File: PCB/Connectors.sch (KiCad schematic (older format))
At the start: 0 parts

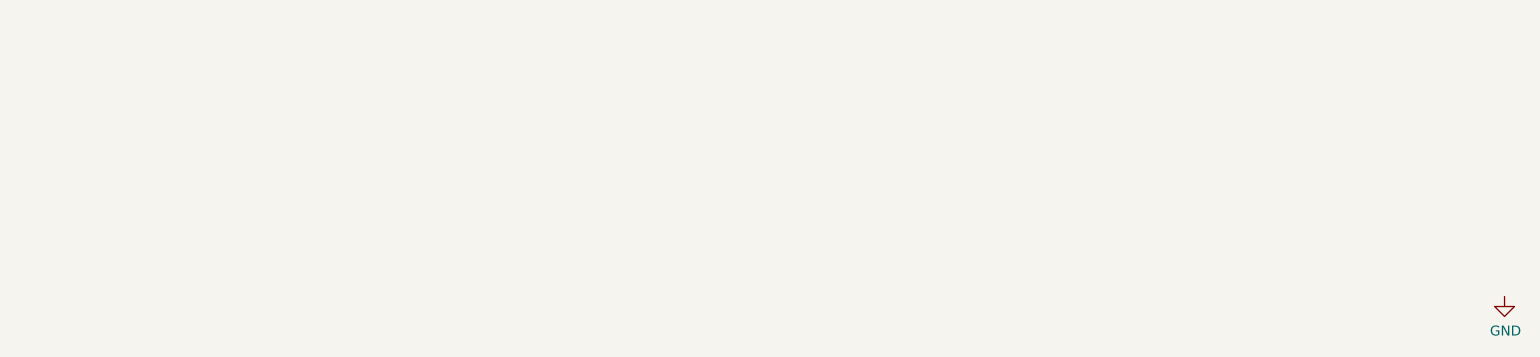
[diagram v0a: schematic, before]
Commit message: Added JST-PH connector to schematic
Orientation of JST-PH connector matches Adafruit Li-ion cells
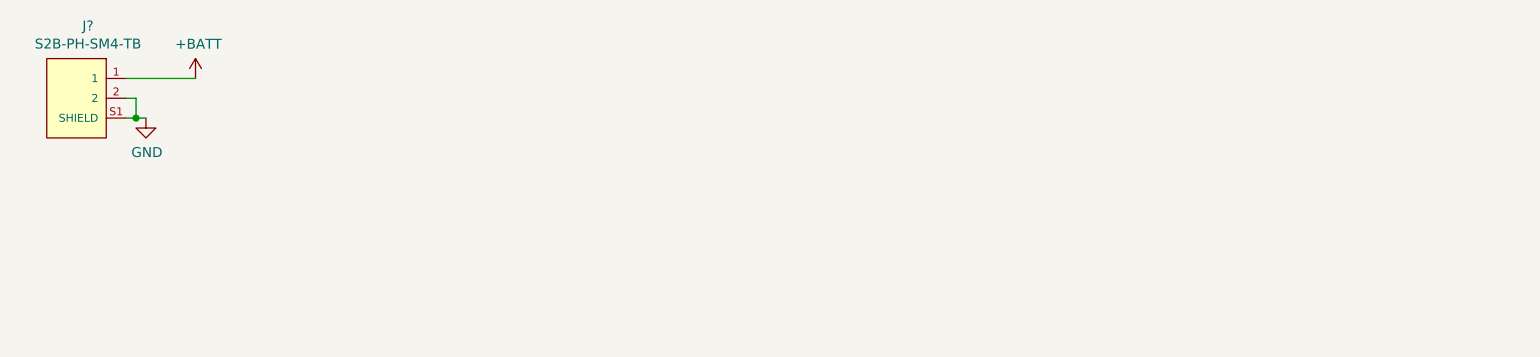
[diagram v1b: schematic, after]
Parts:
- added J?: S2B-PH-SM4-TB, Parts:JST_S2B-PH-SM4-TB, symbol Parts:S2B-PH-SM4-TB
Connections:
- net GND: now also J?.2, J?.S1 (SHIELD), J?.S2 (SHIELD)
- new net +BATT: J?.1
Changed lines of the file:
@@
 L power:GND #PWR?
 U 1 1 5DCE40E5
-P 8850 4100
-F 0 "#PWR?" H 8850 3850 50  0001 C CNN
-F 1 "GND" H 8855 3927 50  0000 C CNN
-F 2 "" H 8850 4100 50  0001 C CNN
-F 3 "" H 8850 4100 50  0001 C CNN
-	1    8850 4100
+P 2000 3200
+F 0 "#PWR?" H 2000 2950 50  0001 C CNN
+F 1 "GND" H 2005 3027 50  0000 C CNN
+F 2 "" H 2000 3200 50  0001 C CNN
+F 3 "" H 2000 3200 50  0001 C CNN
+	1    2000 3200
 	1    0    0    -1
 $EndComp
+$Comp
+L Parts:S2B-PH-SM4-TB J?
+U 1 1 5DCEC85E
+P 1650 3100
+F 0 "J?" H 1592 3465 50  0000 C CNN
+F 1 "S2B-PH-SM4-TB" H 1592 3374 50  0000 C CNN
+F 2 "Parts:JST_S2B-PH-SM4-TB" H 1650 2750 50  0001 C CNN
+F 3 "http://www.jst-mfg.com/product/detail_e.php?series=199" H 1700 3100 50  0001 L BNN
+	1    1650 3100
+	-1   0    0    -1
+$EndComp
+$Comp
+L power:+BATT #PWR?
+U 1 1 5DCED91D
+P 2250 3000
+F 0 "#PWR?" H 2250 2850 50  0001 C CNN
+F 1 "+BATT" H 2265 3173 50  0000 C CNN
+F 2 "" H 2250 3000 50  0001 C CNN
+F 3 "" H 2250 3000 50  0001 C CNN
+	1    2250 3000
+	1    0    0    -1
+$EndComp
+Wire Wire Line
+	1900 3000 2250 3000
+Wire Wire Line
+	1900 3200 1950 3200
+Wire Wire Line
+	1900 3100 1950 3100
+Wire Wire Line
+	1950 3100 1950 3200
+Connection ~ 1950 3200
+Wire Wire Line
+	1950 3200 2000 3200
 $EndSCHEMATC

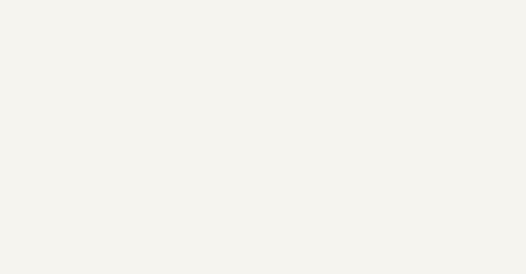
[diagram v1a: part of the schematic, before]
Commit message: Added "near radio" warning to microcontroller pins, connected more ICs to power rails, added transducer capacitive coupling
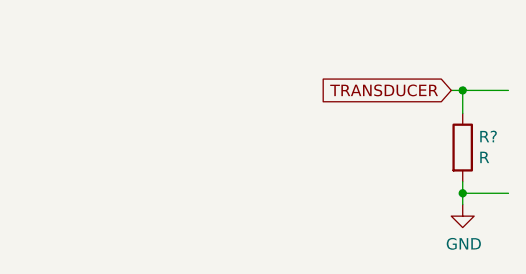
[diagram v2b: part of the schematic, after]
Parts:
- added R?: R, symbol Device:R
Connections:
- net labels added: TRANSDUCER
- wire segments 5 -> 11
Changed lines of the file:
@@
 $EndDescr
 $Comp
-L power:GND #PWR?
+L power:GND #PWR0130
 U 1 1 5DCE40E5
 P 2000 3200
-F 0 "#PWR?" H 2000 2950 50  0001 C CNN
+F 0 "#PWR0130" H 2000 2950 50  0001 C CNN
 F 1 "GND" H 2005 3027 50  0000 C CNN
 F 2 "" H 2000 3200 50  0001 C CNN
@@
 $EndComp
 $Comp
-L power:+BATT #PWR?
+L power:+BATT #PWR0131
 U 1 1 5DCED91D
 P 2250 3000
-F 0 "#PWR?" H 2250 2850 50  0001 C CNN
+F 0 "#PWR0131" H 2250 2850 50  0001 C CNN
 F 1 "+BATT" H 2265 3173 50  0000 C CNN
 F 2 "" H 2250 3000 50  0001 C CNN
@@
 Wire Wire Line
 	1950 3200 2000 3200
+Text GLabel 8400 3000 0    50   Input ~ 0
+TRANSDUCER
+$Comp
+L Device:R R?
+U 1 1 5DE80022
+P 8450 3250
+F 0 "R?" H 8520 3296 50  0000 L CNN
+F 1 "R" H 8520 3205 50  0000 L CNN
+F 2 "" V 8380 3250 50  0001 C CNN
+F 3 "~" H 8450 3250 50  0001 C CNN
+	1    8450 3250
+	1    0    0    -1
+$EndComp
+Wire Wire Line
+	8400 3000 8450 3000
+Wire Wire Line
+	8450 3000 8450 3100
+$Comp
+L power:GND #PWR?
+U 1 1 5DE80E0C
+P 8450 3500
+F 0 "#PWR?" H 8450 3250 50  0001 C CNN
+F 1 "GND" H 8455 3327 50  0000 C CNN
+F 2 "" H 8450 3500 50  0001 C CNN
+F 3 "" H 8450 3500 50  0001 C CNN
+	1    8450 3500
+	1    0    0    -1
+$EndComp
+Wire Wire Line
+	8450 3400 8450 3450
+Wire Wire Line
+	8450 3000 8650 3000
+Connection ~ 8450 3000
+Wire Wire Line
+	8450 3450 8650 3450
+Connection ~ 8450 3450
+Wire Wire Line
+	8450 3450 8450 3500
 $EndSCHEMATC

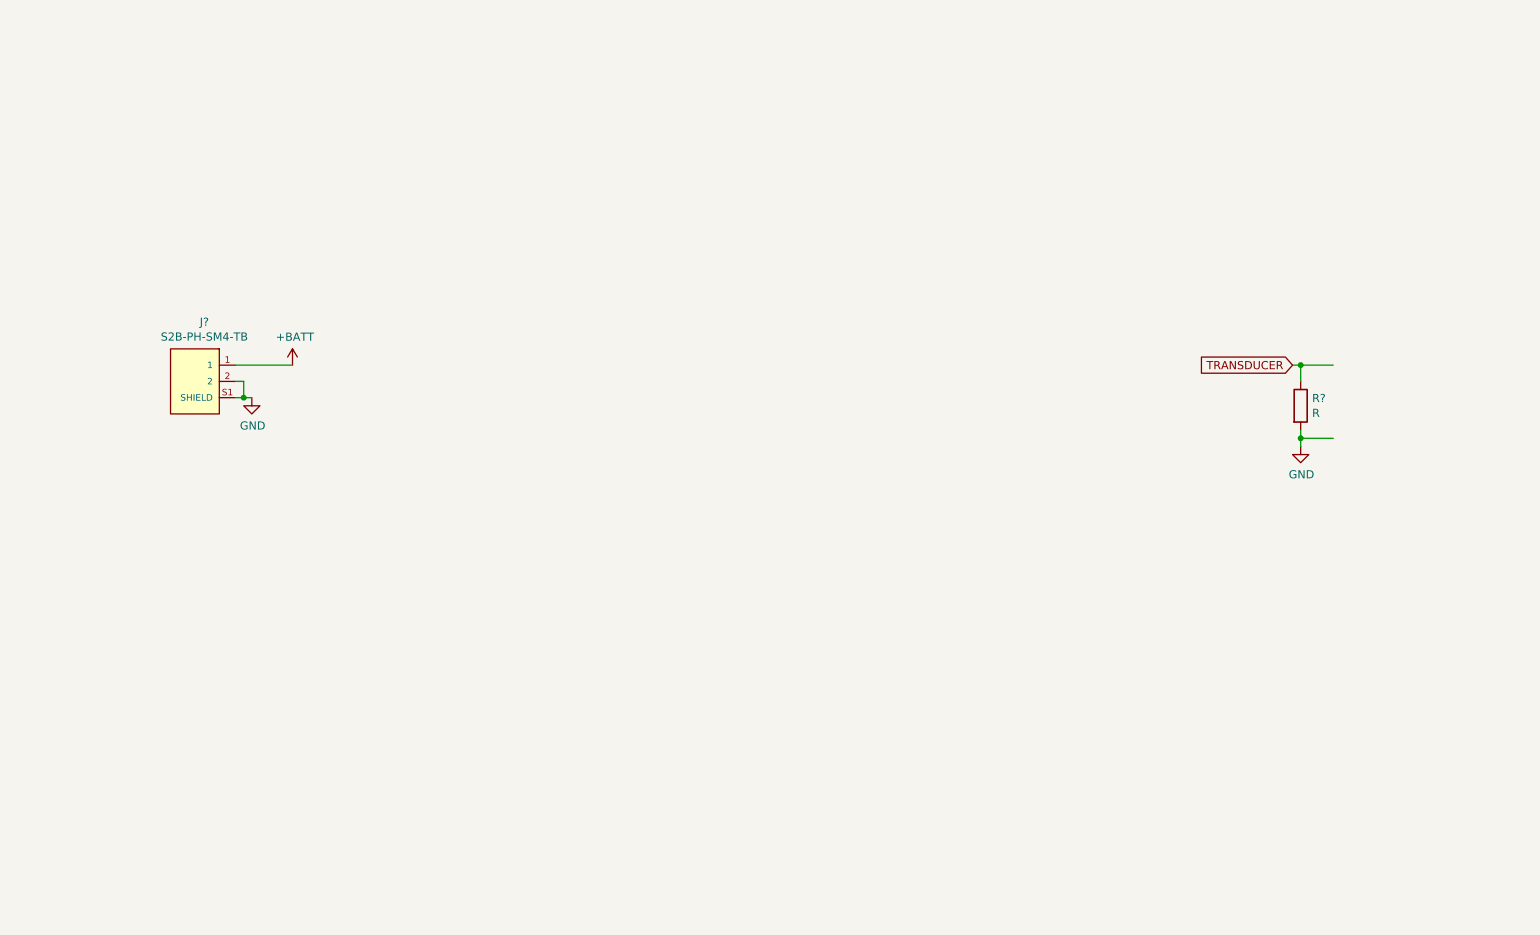
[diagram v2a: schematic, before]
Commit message: Begin adding FPGA connections for JTAG
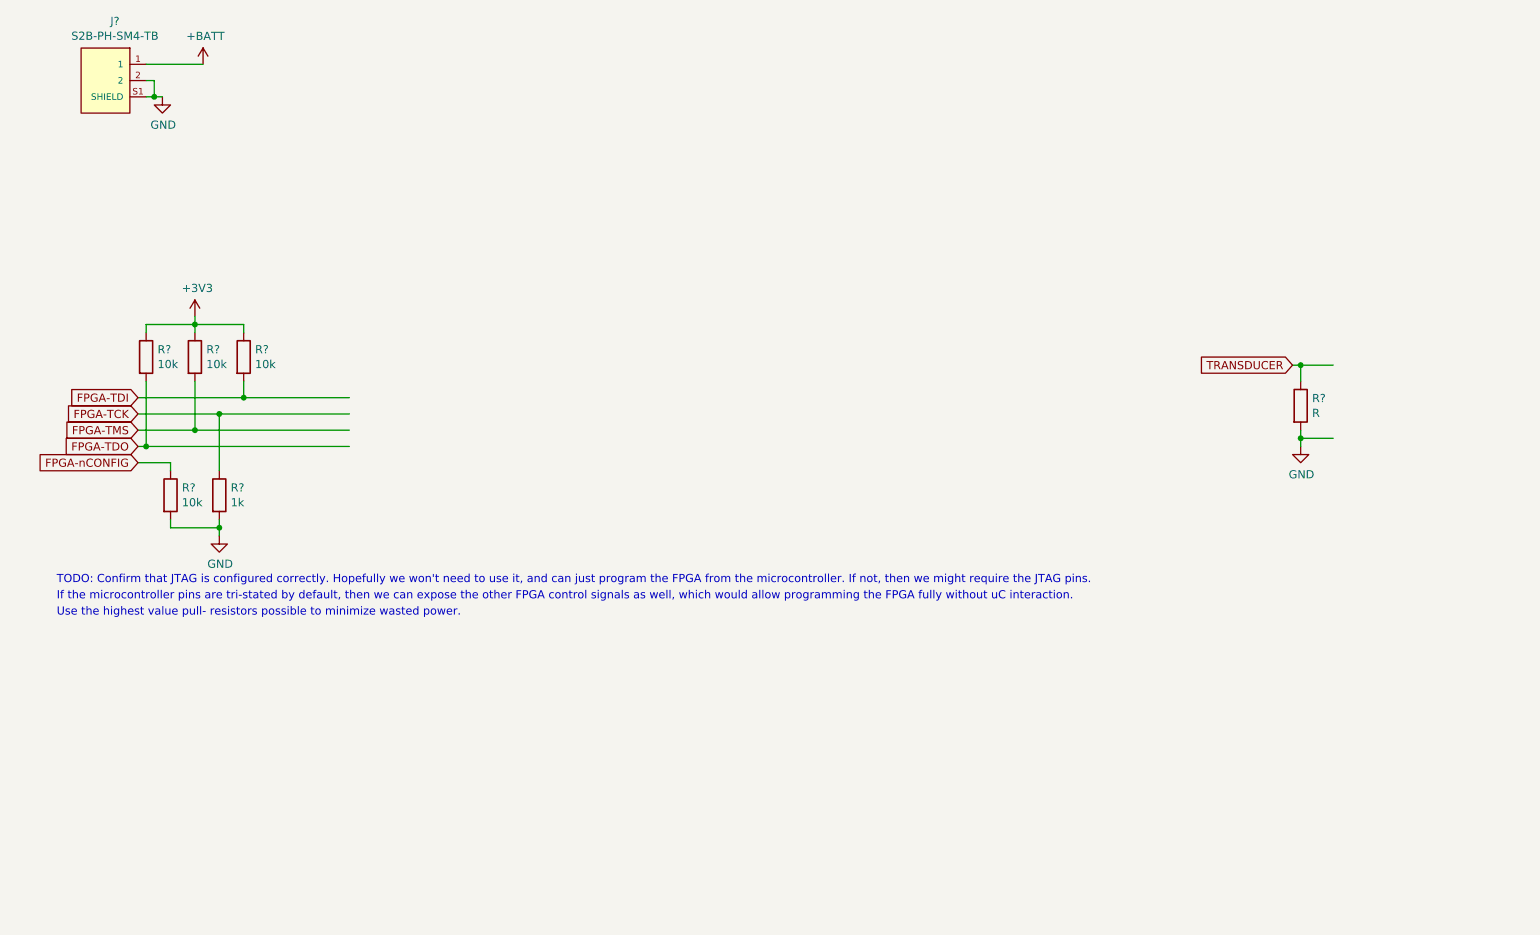
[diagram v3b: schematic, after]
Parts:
- added R?: 1k, symbol Device:R
- added R? (x4): 10k, symbol Device:R
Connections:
- net labels added: +3V3, FPGA-TCK, FPGA-TDI, FPGA-TDO, FPGA-TMS, FPGA-nCONFIG
- wire segments 11 -> 35
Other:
- note added: "If the microcontroller pins are tri-stated by default, then we can expose the other FPGA control signals as well, which would allow programming the FPGA fully without uC interaction."
- note added: "TODO: Confirm that JTAG is configured correctly. Hopefully we won't need to use it, and can just program the FPGA from the microcontroller. If not, then we might require the JTAG pins."
- note added: "Use the highest value pull- resistors possible to minimize wasted power."
- moved on the sheet: J?
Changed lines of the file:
@@
 L power:GND #PWR0130
 U 1 1 5DCE40E5
-P 2000 3200
-F 0 "#PWR0130" H 2000 2950 50  0001 C CNN
-F 1 "GND" H 2005 3027 50  0000 C CNN
-F 2 "" H 2000 3200 50  0001 C CNN
-F 3 "" H 2000 3200 50  0001 C CNN
-	1    2000 3200
+P 1450 1350
+F 0 "#PWR0130" H 1450 1100 50  0001 C CNN
+F 1 "GND" H 1455 1177 50  0000 C CNN
+F 2 "" H 1450 1350 50  0001 C CNN
+F 3 "" H 1450 1350 50  0001 C CNN
+	1    1450 1350
 	1    0    0    -1
 $EndComp
@@
 L Parts:S2B-PH-SM4-TB J?
 U 1 1 5DCEC85E
-P 1650 3100
-F 0 "J?" H 1592 3465 50  0000 C CNN
-F 1 "S2B-PH-SM4-TB" H 1592 3374 50  0000 C CNN
-F 2 "Parts:JST_S2B-PH-SM4-TB" H 1650 2750 50  0001 C CNN
-F 3 "http://www.jst-mfg.com/product/detail_e.php?series=199" H 1700 3100 50  0001 L BNN
-	1    1650 3100
+P 1100 1250
+F 0 "J?" H 1042 1615 50  0000 C CNN
+F 1 "S2B-PH-SM4-TB" H 1042 1524 50  0000 C CNN
+F 2 "Parts:JST_S2B-PH-SM4-TB" H 1100 900 50  0001 C CNN
+F 3 "http://www.jst-mfg.com/product/detail_e.php?series=199" H 1150 1250 50  0001 L BNN
+	1    1100 1250
 	-1   0    0    -1
 $EndComp
@@
 L power:+BATT #PWR0131
 U 1 1 5DCED91D
-P 2250 3000
-F 0 "#PWR0131" H 2250 2850 50  0001 C CNN
-F 1 "+BATT" H 2265 3173 50  0000 C CNN
-F 2 "" H 2250 3000 50  0001 C CNN
-F 3 "" H 2250 3000 50  0001 C CNN
-	1    2250 3000
-	1    0    0    -1
-$EndComp
-Wire Wire Line
-	1900 3000 2250 3000
-Wire Wire Line
-	1900 3200 1950 3200
-Wire Wire Line
-	1900 3100 1950 3100
-Wire Wire Line
-	1950 3100 1950 3200
-Connection ~ 1950 3200
-Wire Wire Line
-	1950 3200 2000 3200
+P 1700 1150
+F 0 "#PWR0131" H 1700 1000 50  0001 C CNN
+F 1 "+BATT" H 1715 1323 50  0000 C CNN
+F 2 "" H 1700 1150 50  0001 C CNN
+F 3 "" H 1700 1150 50  0001 C CNN
+	1    1700 1150
+	1    0    0    -1
+$EndComp
+Wire Wire Line
+	1350 1150 1700 1150
+Wire Wire Line
+	1350 1350 1400 1350
+Wire Wire Line
+	1350 1250 1400 1250
+Wire Wire Line
+	1400 1250 1400 1350
+Connection ~ 1400 1350
+Wire Wire Line
+	1400 1350 1450 1350
 Text GLabel 8400 3000 0    50   Input ~ 0
 TRANSDUCER
@@
 Wire Wire Line
 	8450 3450 8450 3500
+Text GLabel 1300 3200 0    50   Input ~ 0
+FPGA-TDI
+Text GLabel 1300 3300 0    50   Input ~ 0
+FPGA-TCK
+Text GLabel 1300 3400 0    50   Input ~ 0
+FPGA-TMS
+Text GLabel 1300 3500 0    50   Input ~ 0
+FPGA-TDO
+$Comp
+L Device:R R?
+U 1 1 5DECCF2C
+P 1800 3800
+F 0 "R?" H 1870 3846 50  0000 L CNN
+F 1 "1k" H 1870 3755 50  0000 L CNN
+F 2 "" V 1730 3800 50  0001 C CNN
+F 3 "~" H 1800 3800 50  0001 C CNN
+	1    1800 3800
+	1    0    0    -1
+$EndComp
+$Comp
+L Device:R R?
+U 1 1 5DECD846
+P 1950 2950
+F 0 "R?" H 2020 2996 50  0000 L CNN
+F 1 "10k" H 2020 2905 50  0000 L CNN
+F 2 "" V 1880 2950 50  0001 C CNN
+F 3 "~" H 1950 2950 50  0001 C CNN
+	1    1950 2950
+	1    0    0    -1
+$EndComp
+$Comp
+L Device:R R?
+U 1 1 5DECDBAC
+P 1650 2950
+F 0 "R?" H 1720 2996 50  0000 L CNN
+F 1 "10k" H 1720 2905 50  0000 L CNN
+F 2 "" V 1580 2950 50  0001 C CNN
+F 3 "~" H 1650 2950 50  0001 C CNN
+	1    1650 2950
+	1    0    0    -1
+$EndComp
+$Comp
+L power:GND #PWR?
+U 1 1 5DECF0AC
+P 1800 4050
+F 0 "#PWR?" H 1800 3800 50  0001 C CNN
+F 1 "GND" H 1805 3877 50  0000 C CNN
+F 2 "" H 1800 4050 50  0001 C CNN
+F 3 "" H 1800 4050 50  0001 C CNN
+	1    1800 4050
+	1    0    0    -1
+$EndComp
+Wire Wire Line
+	1800 4050 1800 4000
+$Comp
+L power:+3V3 #PWR?
+U 1 1 5DED008E
+P 1650 2700
+F 0 "#PWR?" H 1650 2550 50  0001 C CNN
+F 1 "+3V3" H 1665 2873 50  0000 C CNN
+F 2 "" H 1650 2700 50  0001 C CNN
+F 3 "" H 1650 2700 50  0001 C CNN
+	1    1650 2700
+	1    0    0    -1
+$EndComp
+Wire Wire Line
+	1650 3400 1650 3100
+Wire Wire Line
+	1950 3200 1950 3100
+Wire Wire Line
+	1650 2800 1650 2750
+Wire Wire Line
+	1650 2750 1950 2750
+Wire Wire Line
+	1950 2750 1950 2800
+Wire Wire Line
+	1650 2700 1650 2750
+Connection ~ 1650 2750
+Wire Wire Line
+	1950 3200 2600 3200
+Connection ~ 1950 3200
+Wire Wire Line
+	1650 3400 2600 3400
+Connection ~ 1650 3400
+Connection ~ 1800 3300
+Wire Wire Line
+	1800 3300 2600 3300
+Text Notes 800  4350 0    50   ~ 0
+TODO: Confirm that JTAG is configured correctly. Hopefully we won't need to use it, and can just program the FPGA from the microcontroller. If not, then we might require the JTAG pins.
+Text Notes 800  4450 0    50   ~ 0
+If the microcontroller pins are tri-stated by default, then we can expose the other FPGA control signals as well, which would allow programming the FPGA fully without uC interaction.
+Text Notes 800  4550 0    50   ~ 0
+Use the highest value pull- resistors possible to minimize wasted power.
+Text GLabel 1300 3600 0    50   Input ~ 0
+FPGA-nCONFIG
+$Comp
+L Device:R R?
+U 1 1 5DFBD8B8
+P 1350 2950
+F 0 "R?" H 1420 2996 50  0000 L CNN
+F 1 "10k" H 1420 2905 50  0000 L CNN
+F 2 "" V 1280 2950 50  0001 C CNN
+F 3 "~" H 1350 2950 50  0001 C CNN
+	1    1350 2950
+	1    0    0    -1
+$EndComp
+Wire Wire Line
+	1300 3200 1950 3200
+Wire Wire Line
+	1300 3300 1800 3300
+Wire Wire Line
+	1300 3400 1650 3400
+Wire Wire Line
+	1350 2800 1350 2750
+Wire Wire Line
+	1350 2750 1650 2750
+Wire Wire Line
+	1350 3100 1350 3500
+Wire Wire Line
+	1300 3500 1350 3500
+Connection ~ 1350 3500
+Wire Wire Line
+	1350 3500 2600 3500
+$Comp
+L Device:R R?
+U 1 1 5DFC540A
+P 1500 3800
+F 0 "R?" H 1570 3846 50  0000 L CNN
+F 1 "10k" H 1570 3755 50  0000 L CNN
+F 2 "" V 1430 3800 50  0001 C CNN
+F 3 "~" H 1500 3800 50  0001 C CNN
+	1    1500 3800
+	1    0    0    -1
+$EndComp
+Wire Wire Line
+	1800 4000 1500 4000
+Wire Wire Line
+	1500 4000 1500 3950
+Connection ~ 1800 4000
+Wire Wire Line
+	1800 4000 1800 3950
+Wire Wire Line
+	1500 3600 1300 3600
+Wire Wire Line
+	1500 3600 1500 3650
+Wire Wire Line
+	1800 3300 1800 3650
 $EndSCHEMATC

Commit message: Add debug headers for FPGA and microcontroller
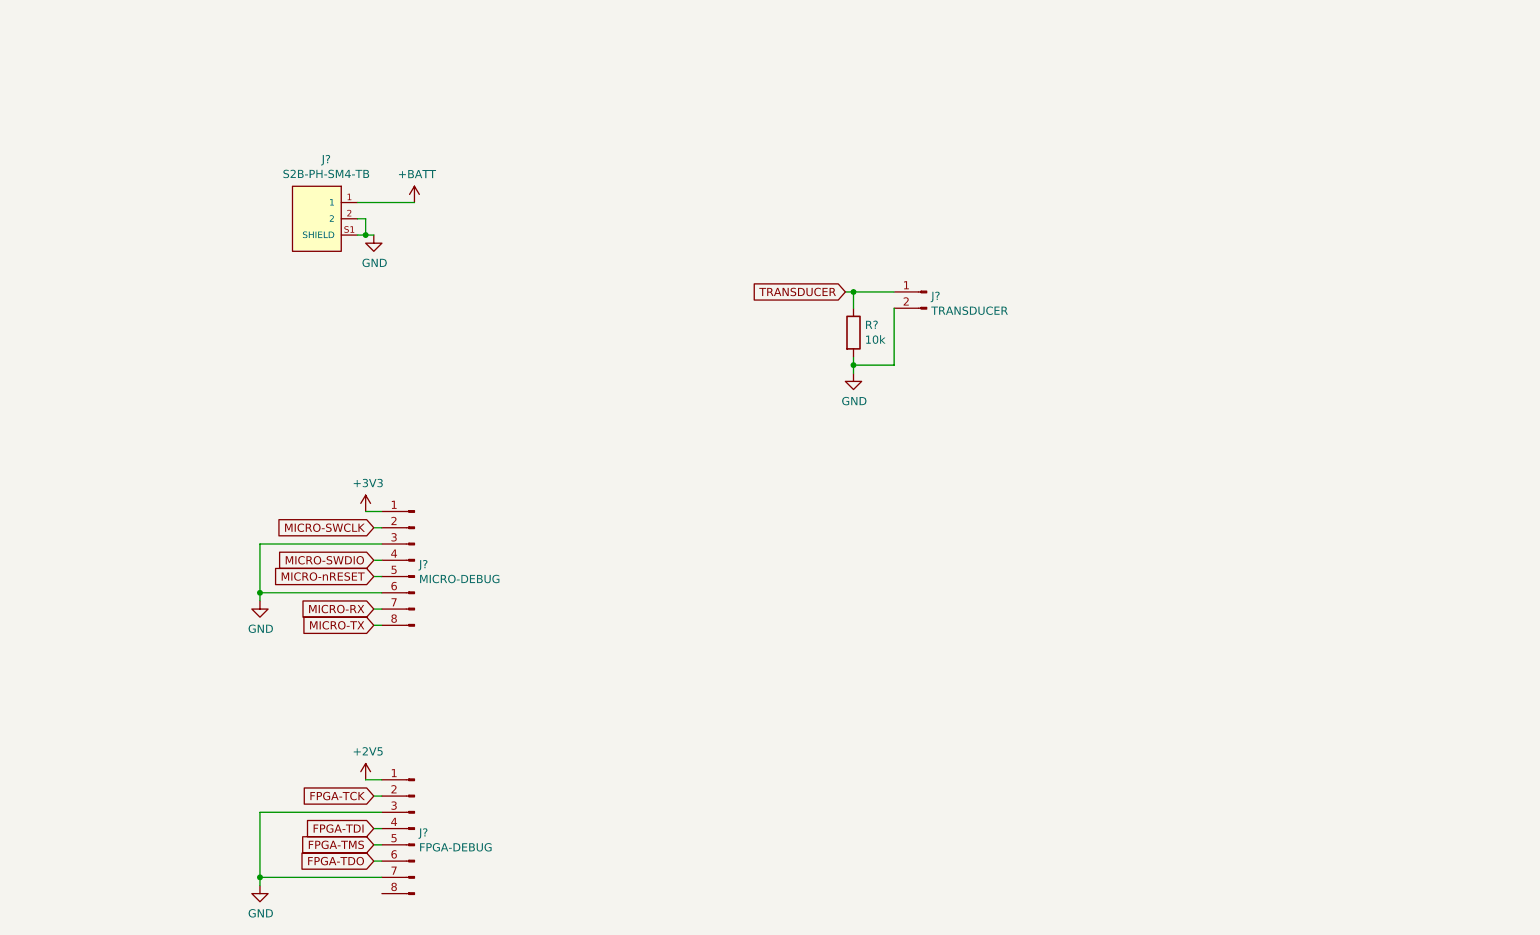
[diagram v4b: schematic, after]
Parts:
- removed R?: 1k, symbol Device:R
- removed R? (x4): 10k, symbol Device:R
- added J?: MICRO-DEBUG, Pin_Headers:Pin_Header_Straight_1x08_Pitch2.54mm, symbol Connector:Conn_01x08_Male
- added J?: FPGA-DEBUG, Pin_Headers:Pin_Header_Straight_1x08_Pitch2.54mm, symbol Connector:Conn_01x08_Male
- added J?: TRANSDUCER, Pin_Headers:Pin_Header_Straight_1x02_Pitch2.54mm, symbol Connector:Conn_01x02_Male
- R?: value R -> 10k; footprint (none) -> Resistors_SMD:R_1206_HandSoldering
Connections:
- net labels added: +2V5, MICRO-RX, MICRO-SWCLK, MICRO-SWDIO, MICRO-TX, MICRO-nRESET
- net labels removed: FPGA-nCONFIG
- wire segments 35 -> 31
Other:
- note removed: "If the microcontroller pins are tri-stated by default, then we can expose the other FPGA control signals as well, which would allow programming the FPGA fully without uC interaction."
- note removed: "TODO: Confirm that JTAG is configured correctly. Hopefully we won't need to use it, and can just program the FPGA from the microcontroller. If not, then we might require the JTAG pins."
- note removed: "Use the highest value pull- resistors possible to minimize wasted power."
- moved on the sheet: J?, R?
